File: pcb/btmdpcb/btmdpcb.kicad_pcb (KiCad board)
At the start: 4 copper layers, 72.4 x 44.4 mm, 115 parts, among them J1 USB_C_Receptacle_USB2.0_16P, Q1 BSD235N, Q2 BSD235C, Q3 BSD235N, Q4 BSD235C, Q5 AO3401A, Q6 BSD235C, T1 ED8_4, T2 ED8_4, U1 LM393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

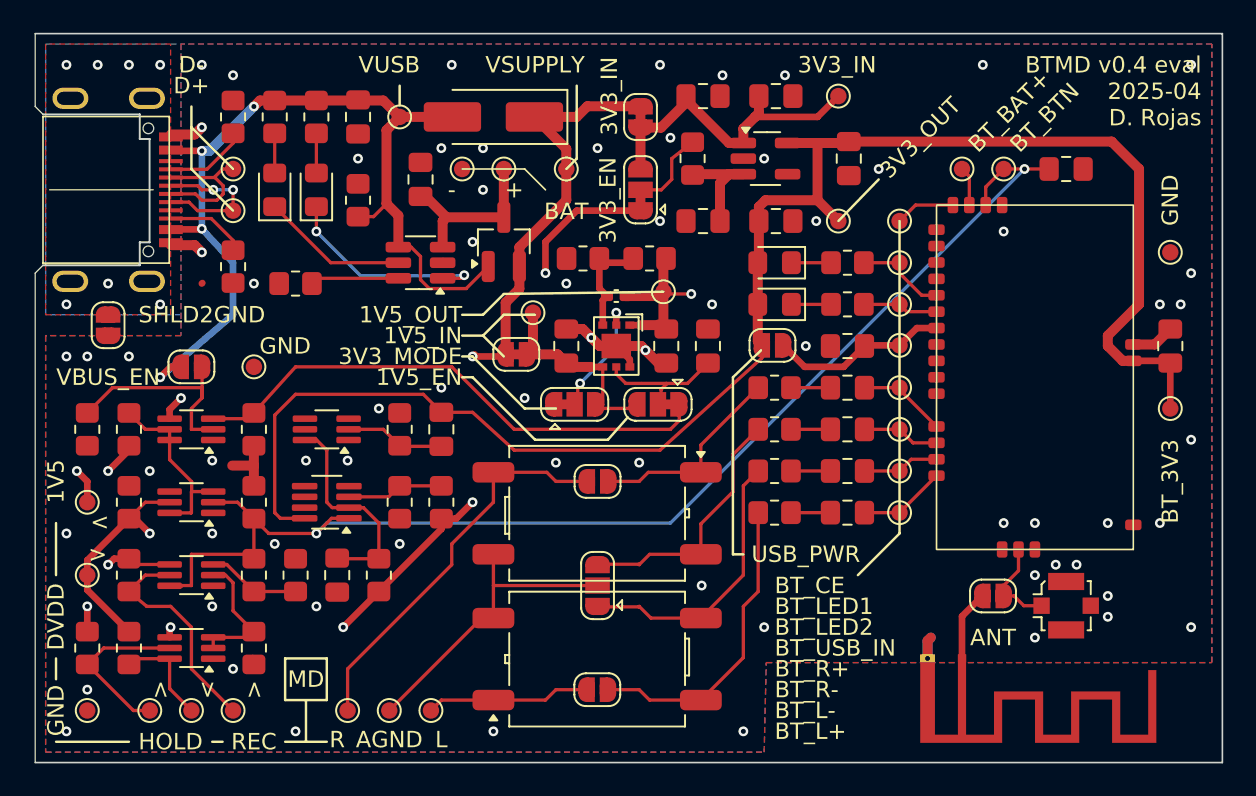
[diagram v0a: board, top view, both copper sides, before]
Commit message: Fix connectors & clearance; touch up PCB
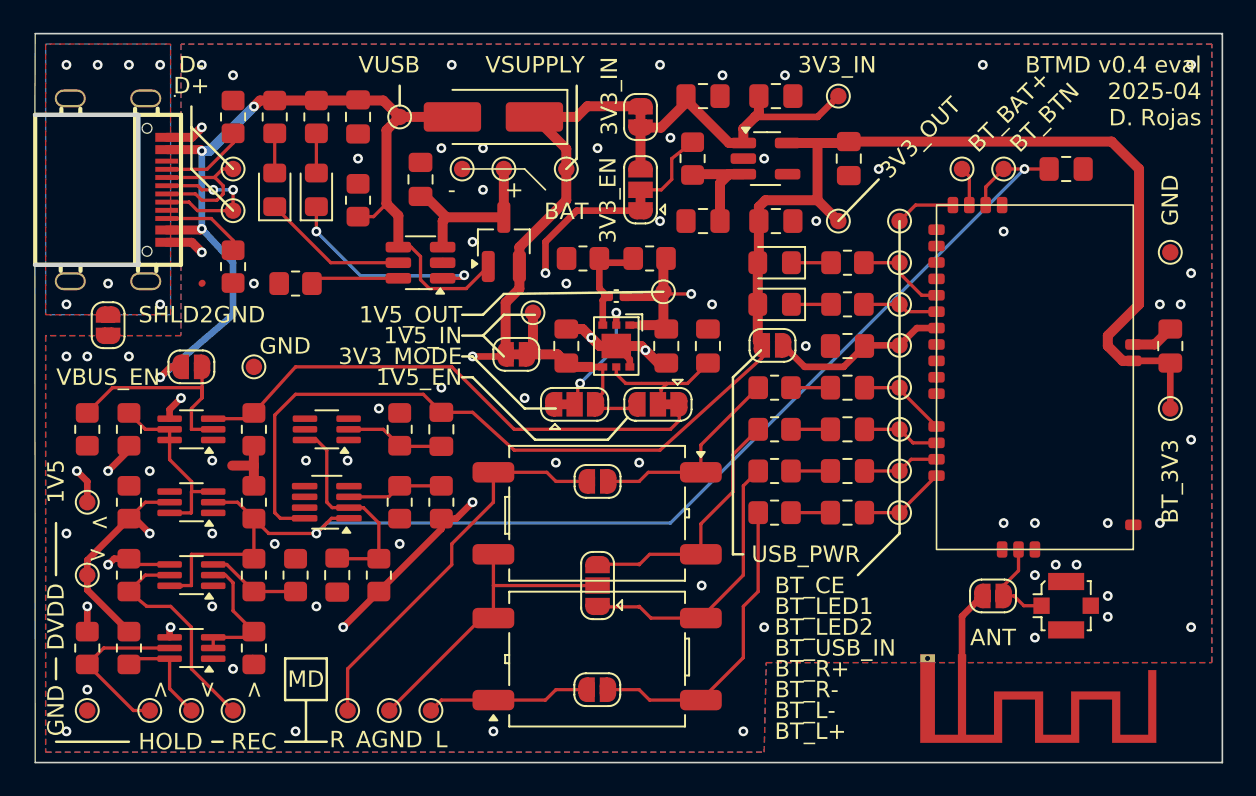
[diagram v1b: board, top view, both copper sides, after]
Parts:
- J2: renamed from J1; footprint usb:TYPE-C-31-M-14 -> usb:USB-C-SMD_12P-P0.50-H-F_TYPE-C-31-M-14
- moved J2 1.91 mm to (101.0, 50.8)
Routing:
- net GND: track 25.7 -> 20.7 mm
- net /supply/D-: track 8.77 -> 9.33 mm
- net /supply/D+: track 9.17 -> 9.68 mm
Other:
- outline, holes or cut-outs redrawn
